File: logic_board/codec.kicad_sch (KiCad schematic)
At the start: 40 parts, among them J1 SJ3-35083C-TR, J4 Conn_01x02, U2 ES8388, U6 TLV9061xDBV

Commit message: Added ferrite on codec analog power supply.
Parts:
- added FB1: Murata BLM18HE601SN1D, Inductor_SMD:L_0603_1608Metric, symbol Device:FerriteBead_Small
- C10, C4: value 47uF -> 100uF
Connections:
- net +3V3: now also FB1.1; no longer C14.1, C5.1
- net at C13.1, D5.1 (K), J1.1: now also C4.2; no longer R10.1
- net at C12.1, D4.1 (K), J1.5: now also C10.2; no longer R11.1
- net at R10.2: now also U2.12 (LOUT1); no longer C4.2
- net at R11.2: now also U2.11 (ROUT1); no longer C10.2
- net at C4.1: now also R10.1; no longer U2.12 (LOUT1)
- net at C10.1: now also R11.1; no longer U2.11 (ROUT1)
- new net: C14.1, C5.1, FB1.2
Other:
- moved on the sheet: C14, C31, C39, C5, C6, C7, C8, C9, R10, R11

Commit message: Change charger to BQ25185
This one has power steering so it can run the MCU and charge simultaneously without charge termination problems.
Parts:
- R10, R11, R12, R13, R14, R15, R16, R4, R5, R6, R7: symbol Device:R -> Device:R_US
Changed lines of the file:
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@@
 	)
 	(symbol
-		(lib_id "Device:R")
+		(lib_id "Device:R_US")
 		(at 152.4 33.02 90)
 		(unit 1)
@@
 		(dnp no)
 		(property "Reference" "R4"
-			(at 152.4 33.02 90)
+			(at 148.844 31.75 90)
 			(effects
 				(font
@@
 	)
 	(symbol
-		(lib_id "Device:R")
+		(lib_id "Device:R_US")
 		(at 162.56 140.97 90)
 		(unit 1)
@@
 	)
 	(symbol
-		(lib_id "Device:R")
+		(lib_id "Device:R_US")
 		(at 162.56 148.59 90)
 		(unit 1)
@@
 		(on_board yes)
 		(dnp no)
-		(fields_autoplaced yes)
 		(property "Reference" "R11"
-			(at 162.56 152.4 90)
+			(at 162.56 144.272 90)
 			(effects
 				(font
@@
 		)
 		(property "Value" "22"
-			(at 162.56 154.94 90)
+			(at 162.56 146.558 90)
 			(effects
 				(font
@@
 	)
 	(symbol
-		(lib_id "Device:R")
+		(lib_id "Device:R_US")
 		(at 114.3 165.1 0)
 		(unit 1)
@@
 		(on_board yes)
 		(dnp no)
-		(fields_autoplaced yes)
 		(property "Reference" "R13"
-			(at 116.84 163.8299 0)
+			(at 116.332 163.83 0)
 			(effects
 				(font
@@
 		)
 		(property "Value" "20"
-			(at 116.84 166.3699 0)
+			(at 116.84 166.116 0)
 			(effects
 				(font
@@
 	)
 	(symbol
-		(lib_id "Device:R")
+		(lib_id "Device:R_US")
 		(at 152.4 40.64 90)
 		(unit 1)
@@
 		(dnp no)
 		(property "Reference" "R7"
-			(at 152.4 40.64 90)
+			(at 148.59 39.878 90)
 			(effects
 				(font
@@
 	)
 	(symbol
-		(lib_id "Device:R")
+		(lib_id "Device:R_US")
 		(at 73.66 100.33 90)
 		(unit 1)
@@
 	)
 	(symbol
-		(lib_id "Device:R")
+		(lib_id "Device:R_US")
 		(at 152.4 38.1 90)
 		(unit 1)
@@
 		(dnp no)
 		(property "Reference" "R6"
-			(at 152.4 38.1 90)
+			(at 148.59 37.338 90)
 			(effects
 				(font
@@
 	)
 	(symbol
-		(lib_id "Device:R")
+		(lib_id "Device:R_US")
 		(at 152.4 43.18 90)
 		(unit 1)
@@
 		(dnp no)
 		(property "Reference" "R16"
-			(at 152.4 43.18 90)
+			(at 148.082 42.418 90)
 			(effects
 				(font
@@
 	)
 	(symbol
-		(lib_id "Device:R")
+		(lib_id "Device:R_US")
 		(at 109.22 165.1 0)
 		(unit 1)
@@
 		(on_board yes)
 		(dnp no)
-		(fields_autoplaced yes)
 		(property "Reference" "R15"
-			(at 106.68 163.8299 0)
-			(effects
-				(font
-					(size 1.27 1.27)
-				)
-				(justify right)
+			(at 103.632 164.592 0)
+			(effects
+				(font
+					(size 1.27 1.27)
+				)
+				(justify left)
 			)
 		)
 		(property "Value" "20"
-			(at 106.68 166.3699 0)
-			(effects
-				(font
-					(size 1.27 1.27)
-				)
-				(justify right)
+			(at 104.902 166.624 0)
+			(effects
+				(font
+					(size 1.27 1.27)
+				)
+				(justify left)
 			)
 		)
@@
 	)
 	(symbol
-		(lib_id "Device:R")
+		(lib_id "Device:R_US")
 		(at 152.4 35.56 90)
 		(unit 1)
@@
 		(dnp no)
 		(property "Reference" "R5"
-			(at 152.4 35.56 90)
+			(at 148.844 34.544 90)
 			(effects
 				(font
@@
 	)
 	(symbol
-		(lib_id "Device:R")
+		(lib_id "Device:R_US")
 		(at 96.52 92.71 0)
 		(unit 1)

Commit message: More component placement tweaking, mostly around audio section.
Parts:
- J4: now left out of the parts list

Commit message: Fix JLCPCB issues
- Use fabrication toolkit plugin to fix compnent orientations.
- Add part numbers to all components
- Manually fix some footprint rotation issues and incorrect origins.
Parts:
- C10, C4: LCSC Part Number (none) -> C15008
- C11: LCSC Part Number (none) -> C15849
- C12, C13: value 100nF -> 0.1uF; LCSC Part Number (none) -> C14663
- C14, C15, C33, C34, C39, C9: footprint Capacitor_SMD:C_0603_1608Metric -> Capacitor_SMD:C_0805_2012Metric; LCSC Part Number (none) -> C15850
- C16, C31, C32, C35, C36, C38, C5, C6, C7, C8: footprint Capacitor_SMD:C_0402_1005Metric -> Capacitor_SMD:C_0603_1608Metric; LCSC Part Number (none) -> C14663
- C3: LCSC Part Number (none) -> C1622
- FB1: LCSC Part Number (none) -> C88979
- R10, R11: LCSC Part Number (none) -> C23345
- R12: LCSC Part Number (none) -> C21190
- R13, R15: LCSC Part Number (none) -> C22950
- R14: LCSC Part Number (none) -> C22935
- R16, R4, R5, R6, R7: footprint Resistor_SMD:R_0402_1005Metric -> Resistor_SMD:R_0603_1608Metric; LCSC Part Number (none) -> C23140
- U6: FT Rotation Offset (none) -> 90

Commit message: Fix some PCB issues
TVS diodes had wrong footprint
U5 was rotated 180 degrees in CPL file.
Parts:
- D2, D4, D5: footprint Diode_SMD:D_SOD-882 -> Diode_SMD:D_SOD-323
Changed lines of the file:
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@@
 			)
 		)
-		(property "Footprint" "Diode_SMD:D_SOD-882"
+		(property "Footprint" "Diode_SMD:D_SOD-323"
 			(at 74.93 153.67 0)
 			(effects
@@
 			)
 		)
-		(property "Footprint" "Diode_SMD:D_SOD-882"
+		(property "Footprint" "Diode_SMD:D_SOD-323"
 			(at 57.15 106.68 0)
 			(effects
@@
 			)
 		)
-		(property "Footprint" "Diode_SMD:D_SOD-882"
+		(property "Footprint" "Diode_SMD:D_SOD-323"
 			(at 71.12 153.67 0)
 			(effects

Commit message: Add test points, schematic annotations
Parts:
- removed R16, R4, R5, R6, R7: 33, Resistor_SMD:R_0603_1608Metric, symbol Device:R_US
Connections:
- net ADCDAT: now also U2.8 (ASDOUT)
- net AUDIO_BCLK: now also U2.5 (SCLK)
- net AUDIO_WCLK: now also U2.7 (LRCK)
- net DACDAT: now also U2.6 (DSDIN)
- net MCLK: now also U2.1 (MCLK)
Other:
- note added: "Headphone Output"
- note added: "Input Plug"
- moved on the sheet: C10, C11, C12, C13, C14, C15, C16, C3, C31, C32, C33, C34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

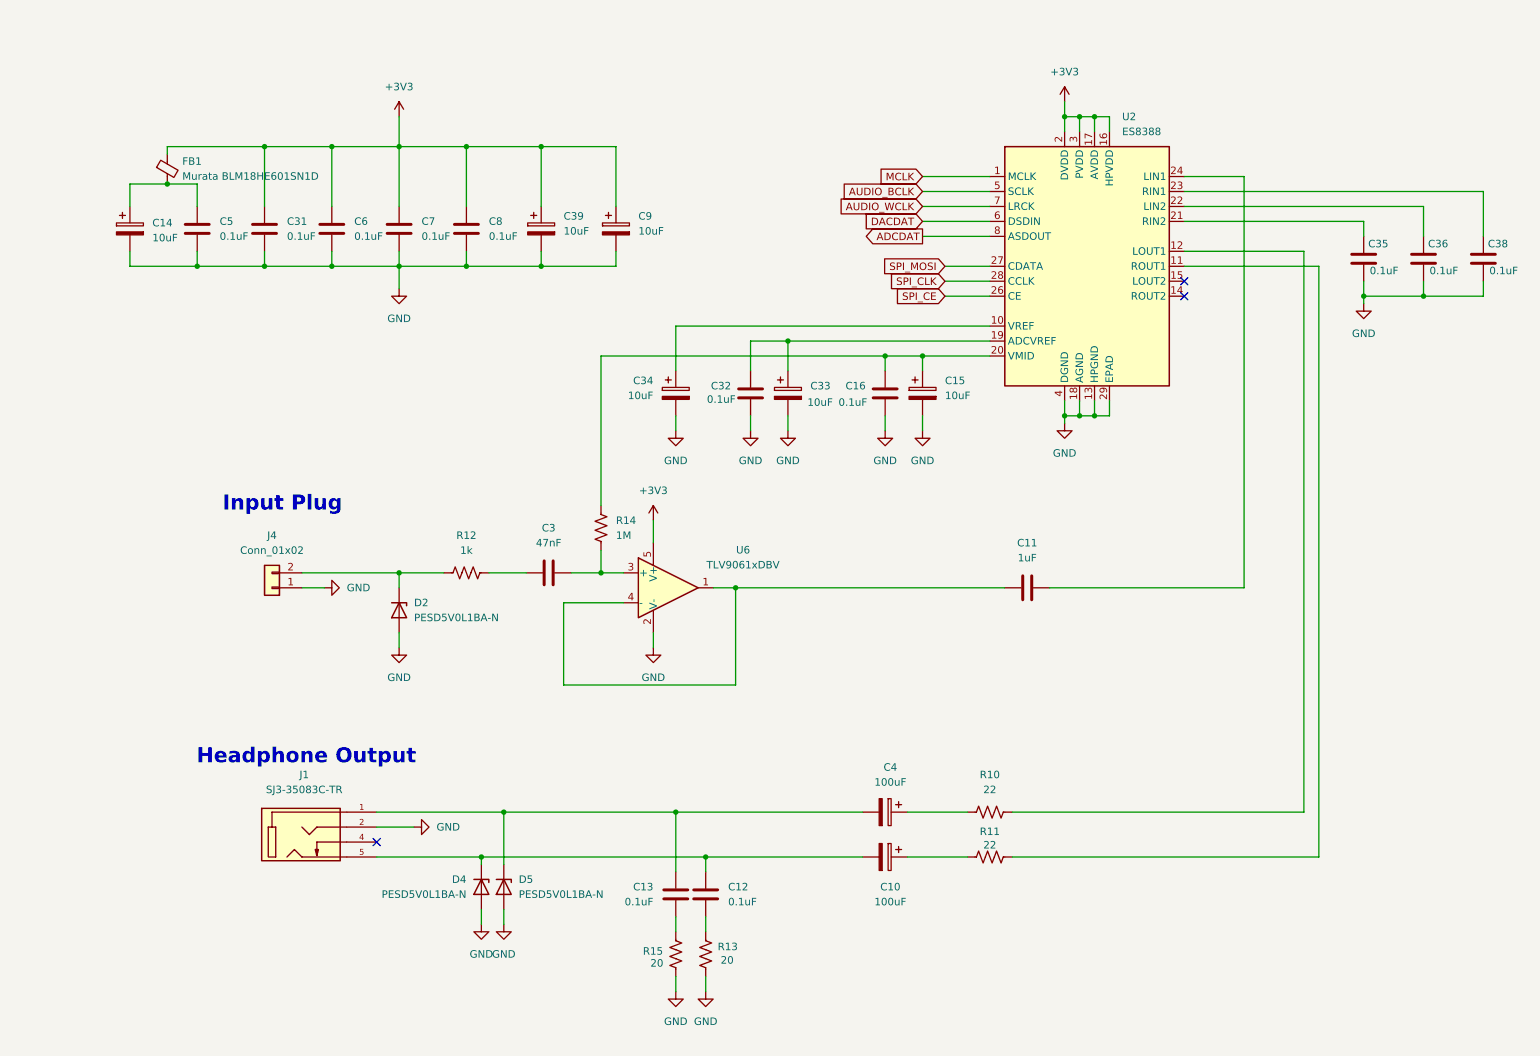
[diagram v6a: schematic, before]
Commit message: Ferrite for codec AVDD was incorrectly placed
It was in parallel the chip instead of in series with the source.
Also fixed ERC warning by adding power flag after buck inductor.
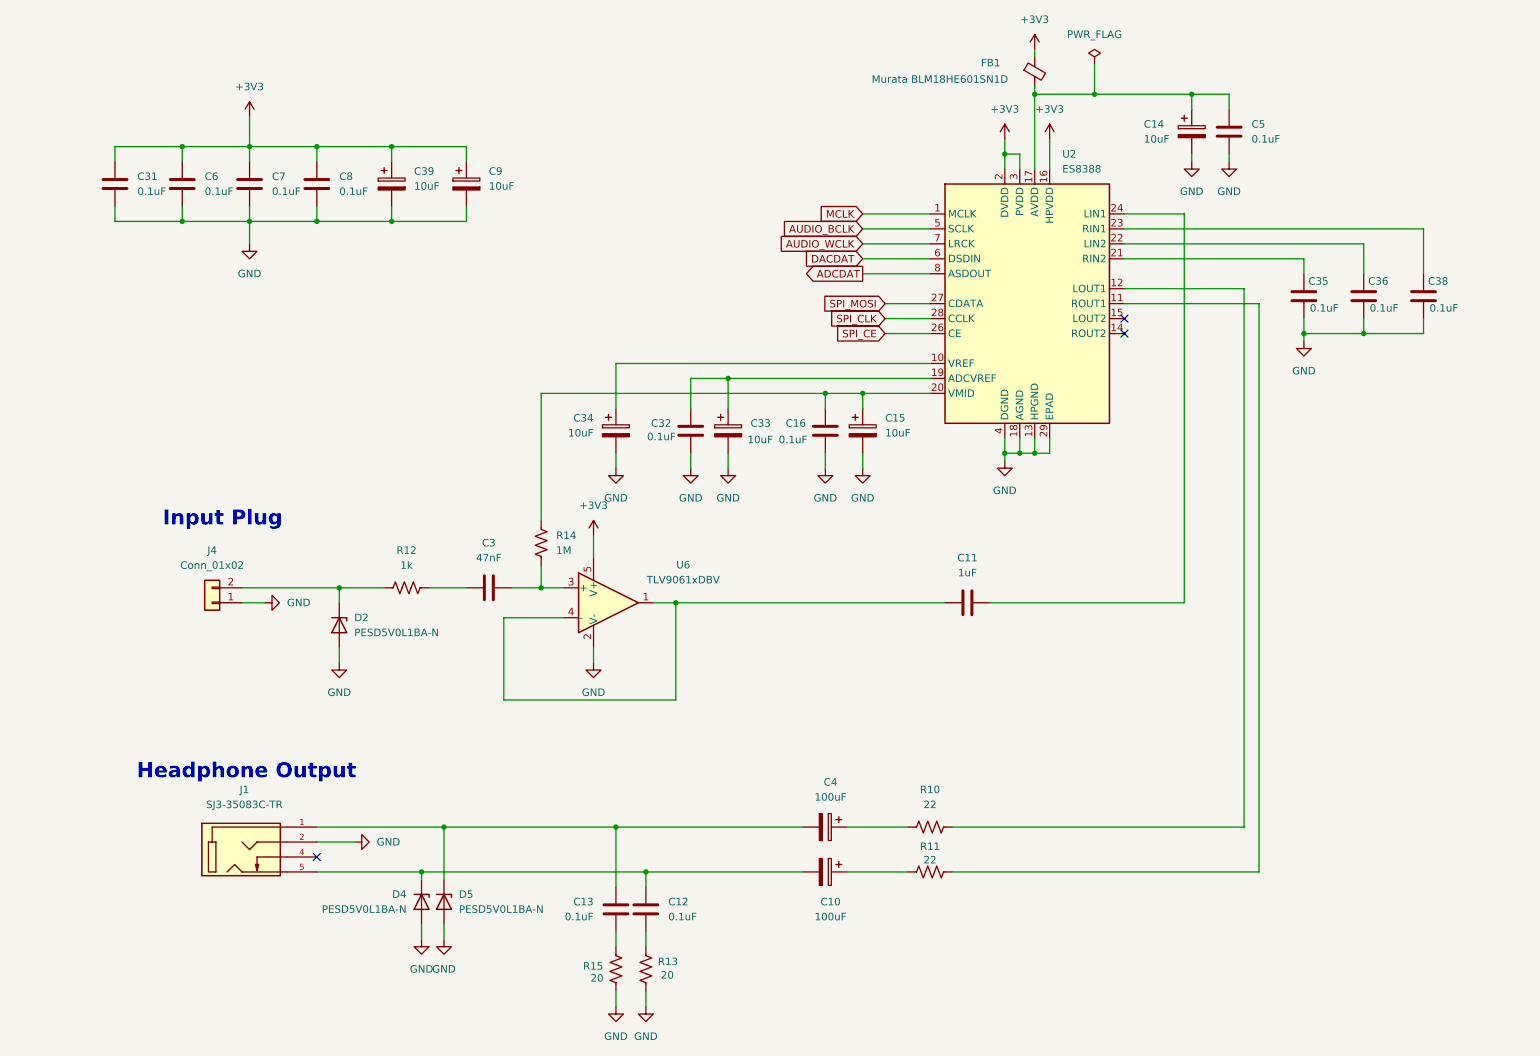
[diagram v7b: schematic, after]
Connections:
- net +3V3: no longer U2.17 (AVDD)
- net at C14.1, C5.1, FB1.2: now also U2.17 (AVDD)
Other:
- moved on the sheet: C10, C11, C12, C13, C14, C15, C16, C3, C31, C32, C33, C34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

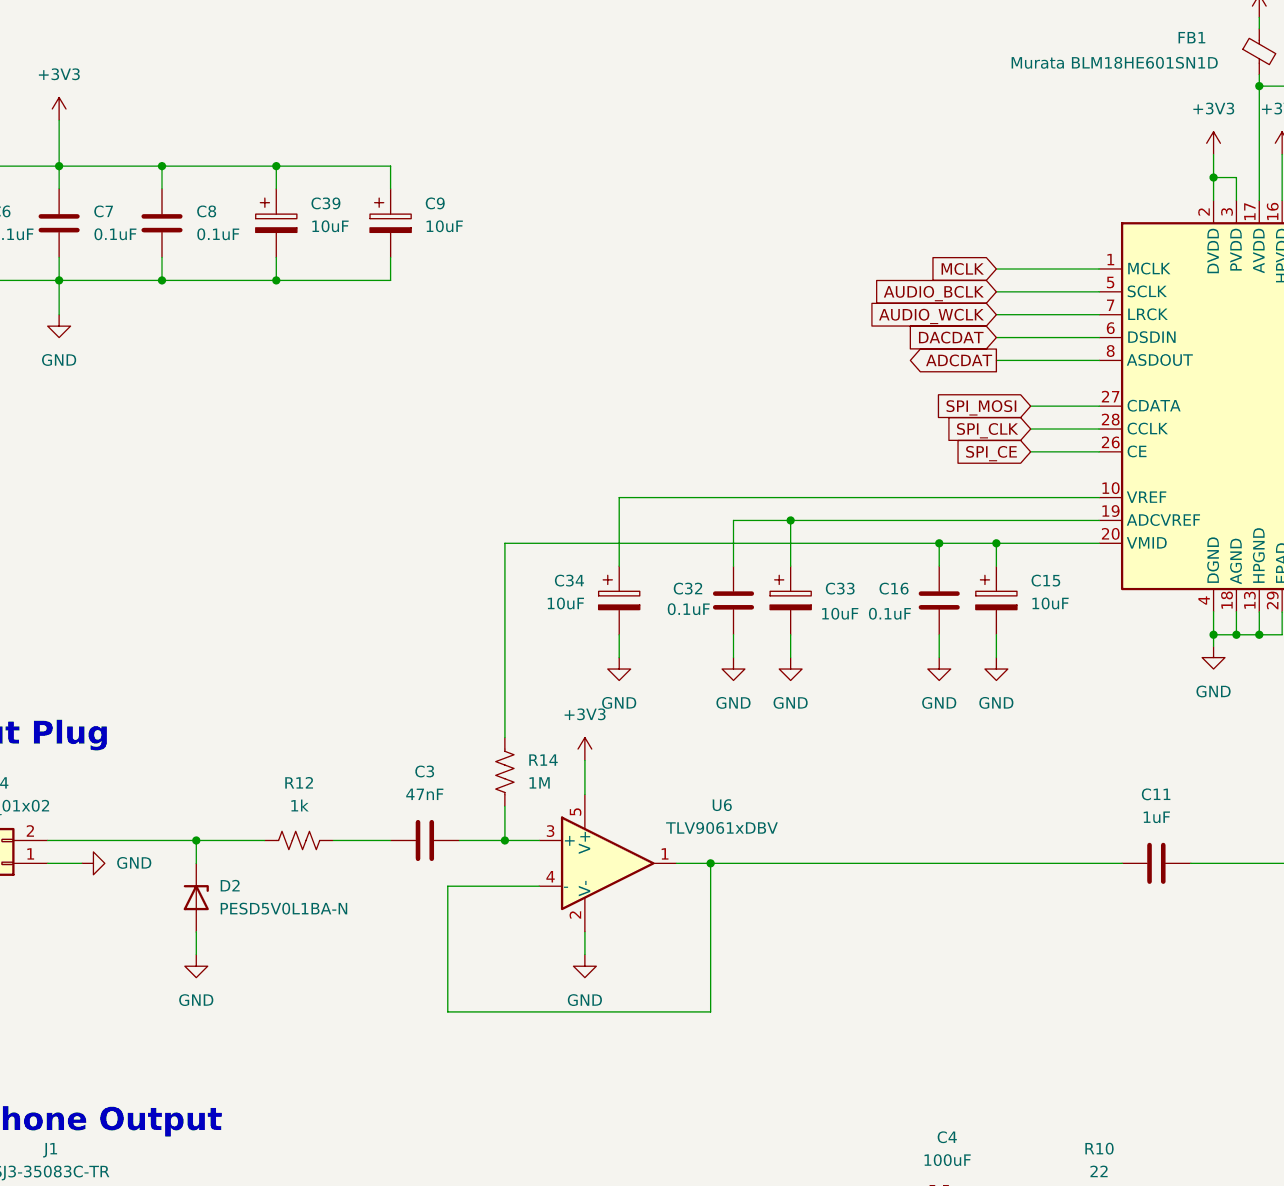
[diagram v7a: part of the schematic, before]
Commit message: Some audio improvements
- Use a separate bias network instead of VMID from the codec.
- Add 100pF cap to ground on op amp input as low pass filter
- Remove bulk 10uF cap from DVDD
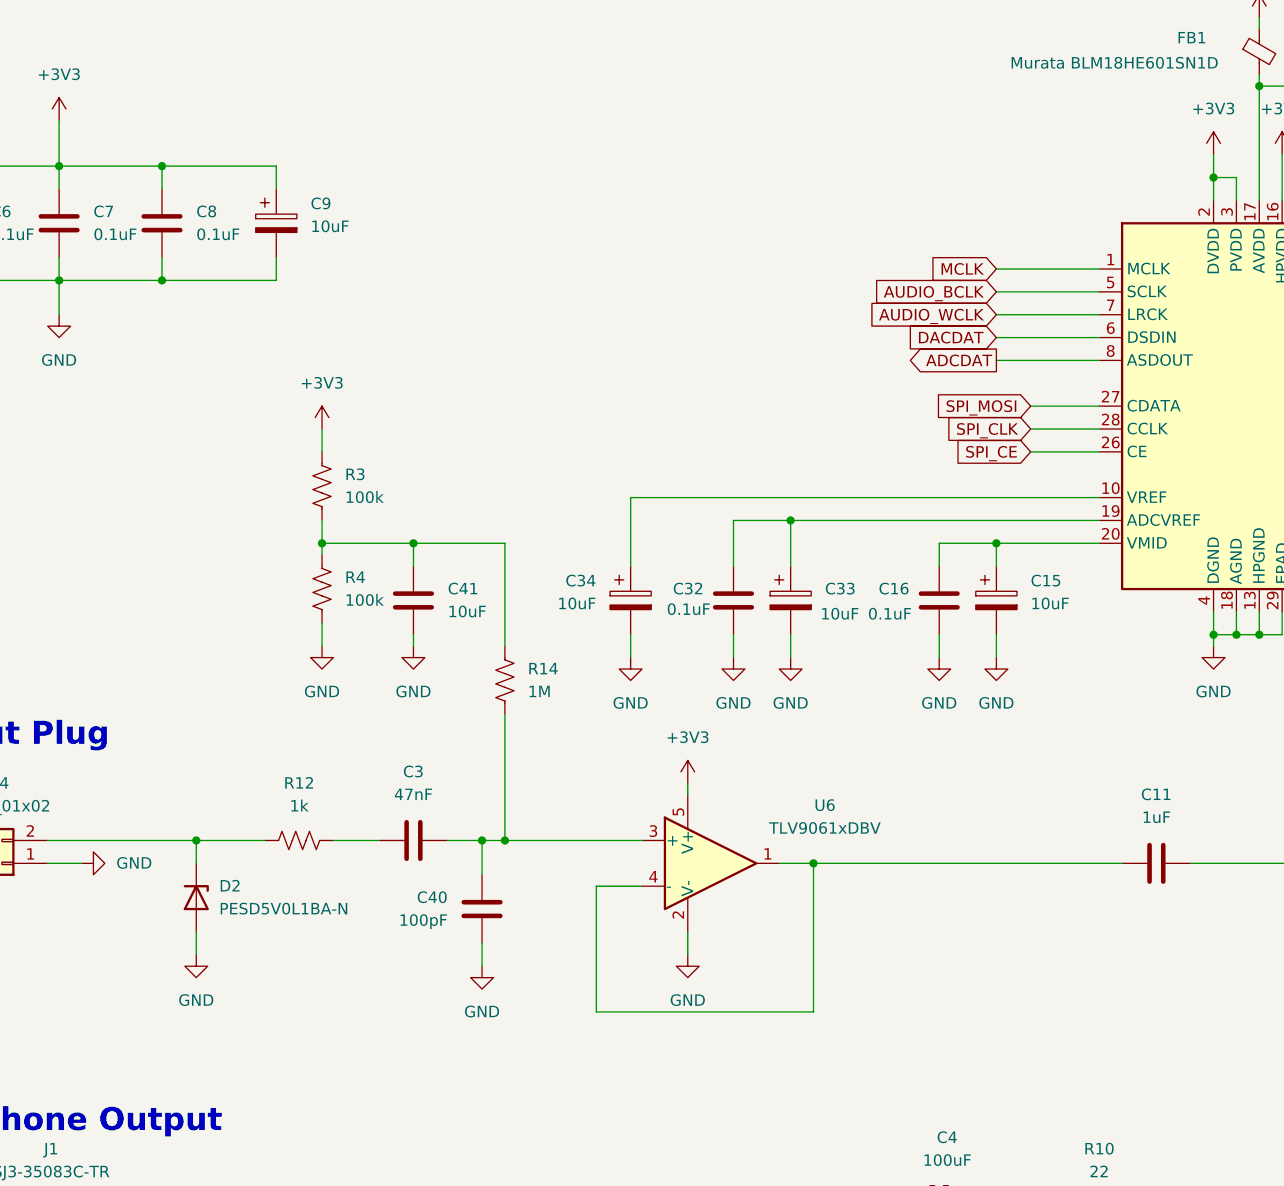
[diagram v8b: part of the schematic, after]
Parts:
- removed C39: 10uF, Capacitor_SMD:C_0805_2012Metric, symbol Device:C_Polarized
- added C40: 100pF, Capacitor_SMD:C_0603_1608Metric, symbol Device:C
- added C41: 10uF, Capacitor_SMD:C_0805_2012Metric, symbol Device:C
- added R3, R4: 100k, Resistor_SMD:R_0603_1608Metric, symbol Device:R_US
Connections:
- net +3V3: now also R3.1
- net GND: now also C40.2, C41.2, R4.2
- net at C15.1, C16.1, U2.20 (VMID): no longer R14.1
- net at C3.2, R14.2, U6.3 (+): now also C40.1
- new net: C41.1, R14.1, R3.2, R4.1
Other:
- moved on the sheet: C3, C34, C9, R14, U6
